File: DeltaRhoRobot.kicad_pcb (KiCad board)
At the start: 4 copper layers, 75 x 100 mm, 121 parts, among them J1 Conn_01x02_Socket, J10 Conn_01x02, J11 Conn_01x08, J12 USB_C_Receptacle_USB2.0, J13 Conn_02x09_Top_Bottom, J14 Conn_01x09, J15 Conn_02x09_Top_Bottom, J2 USB_C_Receptacle_USB2.0, J3 USB_C_Receptacle_USB2.0, J4 B4B-ZRLFSN, J5 B4B-ZRLFSN, J6 Conn_01x09, J7 Conn_02x20_Counter_Clockwise, P1 B6B-ZRLFSN, P2 B6B-ZRLFSN, P3 B6B-ZRLFSN, P4 S6B-ZRLFSN, P5 B6B-ZRLFSN, P6 B6B-ZRLFSN, Q1 MBT3904DW1, Q2 BSS138, Q3 STB55NF06T4, Q5 BSS138, SW1 CAS-120A1, SW4 SW_Push, U1 AP63205WU-7, U10 ICM-20948, U11 FT231XS, U12 ESP32-CAM, U13 MIC5365-3.3YC5, U2 AMS1117-3.3, U3 DRV8835DSSR, U4 RP2040, U5 DRV8835DSSR, U6 DRV8835DSSR, U7 W25X40CLSS, U8 ESP32-S3-WROOM-1-N8R2, Y1 ABM8G-12.000MHZ-4Y-T3

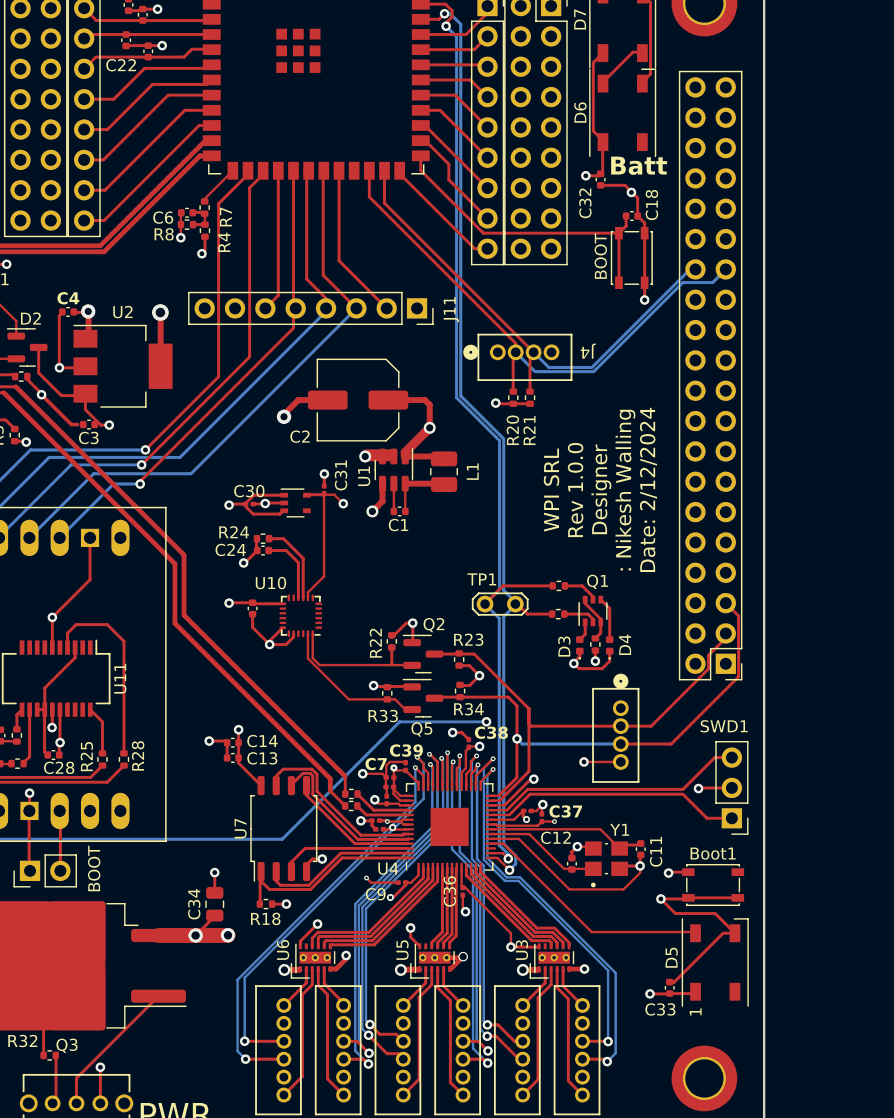
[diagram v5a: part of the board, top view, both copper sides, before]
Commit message: update to I2C
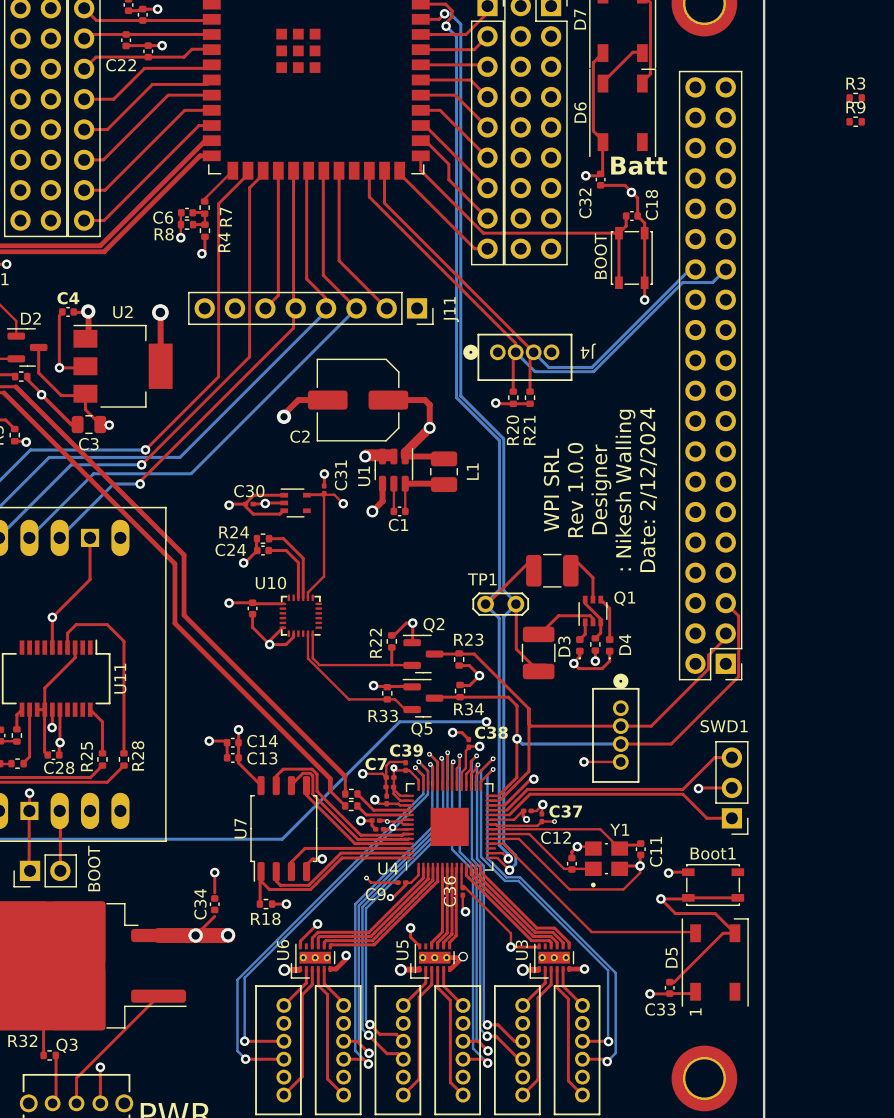
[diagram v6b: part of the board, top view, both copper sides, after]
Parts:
- added R3: 5K, Resistor_SMD:R_0402_1005Metric, F.Cu at (232.7, 62.9)
- added R9: 5K, Resistor_SMD:R_0402_1005Metric, F.Cu at (232.7, 64.9)
- C3: footprint Capacitor_SMD:C_0402_1005Metric -> Capacitor_SMD:C_0805_2012Metric
- C34: footprint Capacitor_SMD:C_0805_2012Metric -> Capacitor_SMD:C_0402_1005Metric
- R12, R13: footprint Resistor_SMD:R_0402_1005Metric -> Resistor_SMD:R_1210_3225Metric_Pad1.30x2.65mm_HandSolder
- moved R13 3.64 mm to (206.1, 109.4), turned to 90 degrees
- moved R12 1.38 mm to (207.3, 102.5)
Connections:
- R12 pad 1: ESP_TX -> Pico_SCL1
- R13 pad 1: ESP_RX -> Pico_SDA1
- R29 pad 2: Net-(U11-USBDM) -> /ESP32-S3-WROOM-1/ESP32CAM/3.3V_Out
- R30 pad 1: Net-(U11-USBDP) -> /ESP32-S3-WROOM-1/ESP32CAM/3.3V_Out
- TP1 pad 1: ESP_RX -> Pico_SDA1
- TP1 pad 2: ESP_TX -> Pico_SCL1
- U11 pad 11: Net-(U11-USBDP) -> /ESP32-S3-WROOM-1/ESP32CAM/3.3V_Out
- U11 pad 12: Net-(U11-USBDM) -> /ESP32-S3-WROOM-1/ESP32CAM/3.3V_Out
- U4 pad 15: ESP_RX -> Pico_SCL1
- U4 pad 16: ESP_TX -> Pico_SDA1
- U8 pad 36: ESP_RX -> Pico_SDA1
- U8 pad 37: ESP_TX -> Pico_SCL1
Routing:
- net Pico_SDA1: track 0.00 -> 86.7 mm, vias 0 -> 2
- net ESP_TX: track 84.7 -> 0.00 mm, vias 2 -> 0
- net Pico_SCL1: track 0.00 -> 84.3 mm, vias 0 -> 2
- net ESP_RX: track 83.2 -> 0.00 mm, vias 2 -> 0
- net /ESP32-S3-WROOM-1/ESP32CAM/3.3V_Out: track 10.8 -> 17.3 mm
- net Net-(U11-USBDM): track 4.73 -> 0.00 mm
- net Net-(Q1A-B1): track 2.85 -> 4.76 mm
- net Net-(U11-USBDP): track 1.83 -> 0.00 mm
- net Net-(Q1B-B2): track 2.97 -> 3.92 mm
- net /Pico/M6_Enc_A: track 36.2 -> 35.6 mm
- net /Pico/M6_Enc_B: track 35.9 -> 36.4 mm
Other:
- board text added: "If UART R=1k"

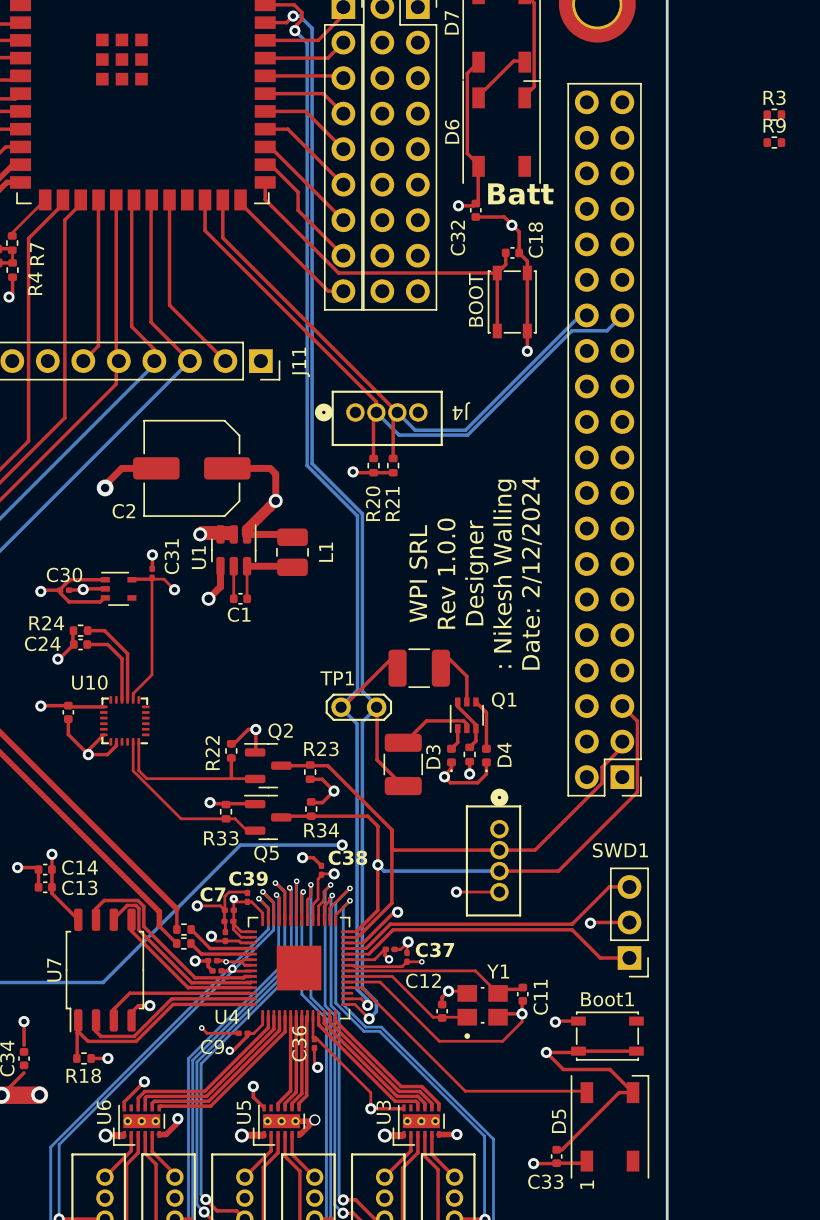
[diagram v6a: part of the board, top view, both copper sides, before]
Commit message: Fixed resistors
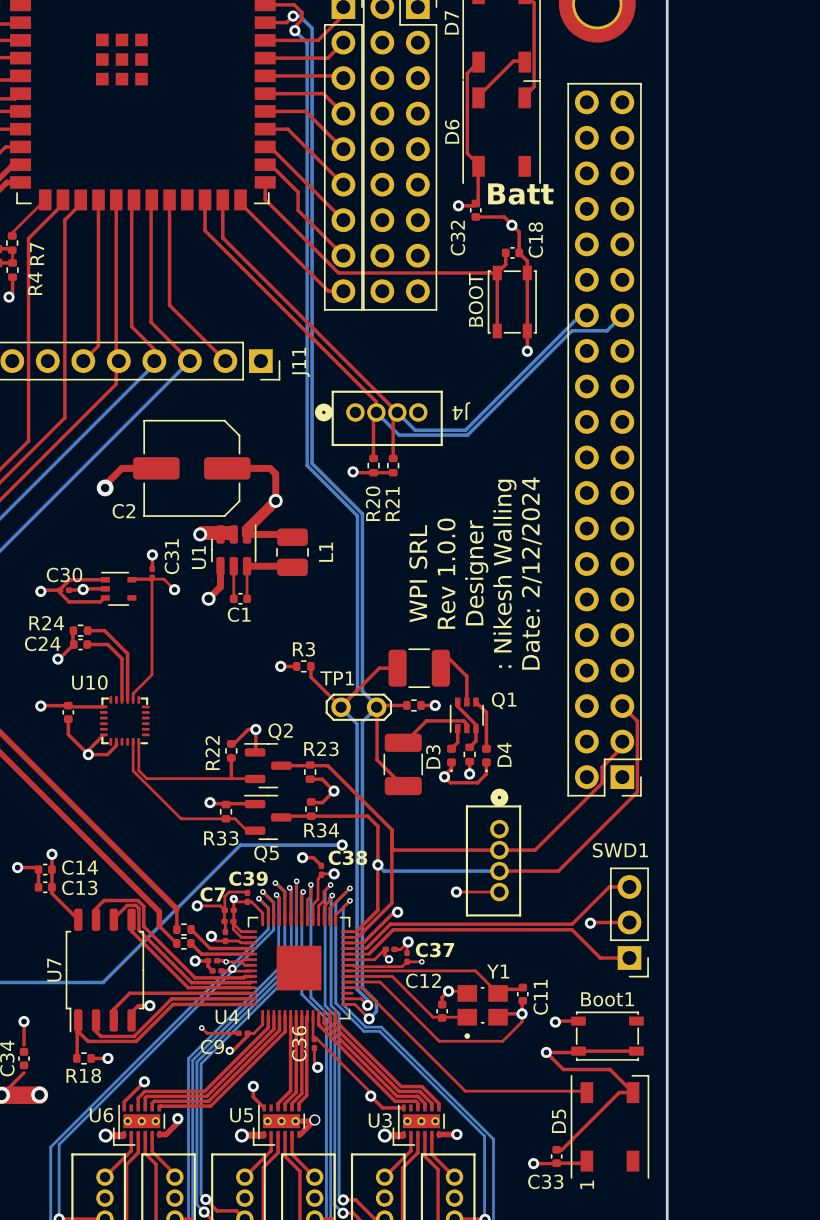
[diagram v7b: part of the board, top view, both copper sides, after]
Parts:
- moved R3 51.9 mm to (199.0, 102.4)
- moved R9 47.8 mm to (206.9, 105.2)
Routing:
- net Pico_SCL1: track 84.3 -> 87.8 mm
- net Pico_SDA1: track 86.7 -> 88.9 mm
- net +3.3V: track 85.9 -> 87.5 mm, vias 18 -> 20

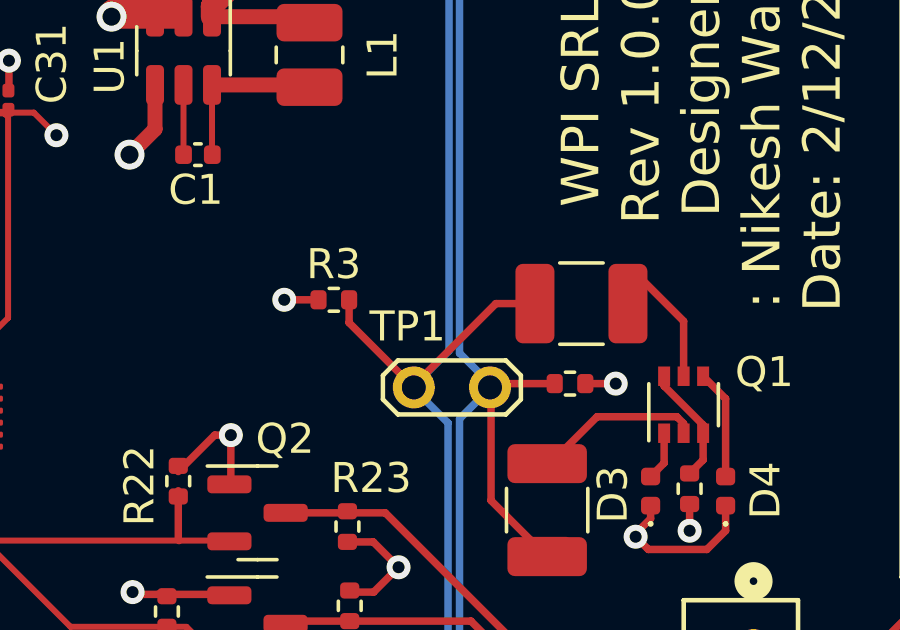
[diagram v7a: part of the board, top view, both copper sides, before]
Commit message: Fixed resistors
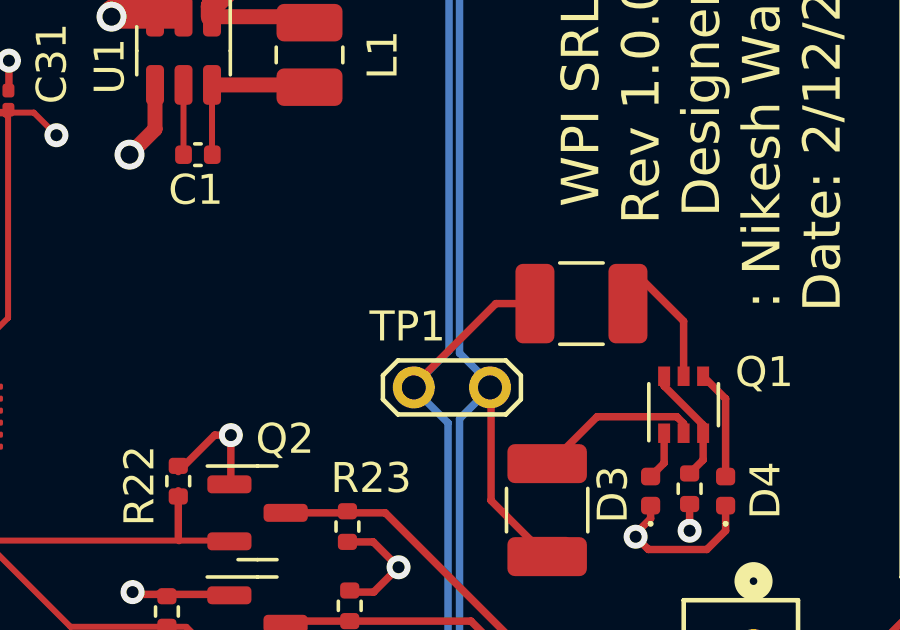
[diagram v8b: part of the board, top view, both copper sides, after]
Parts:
- removed R3, R9: 5K, Resistor_SMD:R_0402_1005Metric
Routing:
- net Pico_SCL1: track 87.8 -> 84.0 mm
- net +3.3V: track 87.5 -> 85.3 mm, vias 20 -> 18
- net Pico_SDA1: track 88.9 -> 86.9 mm
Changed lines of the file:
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@@
     )
   )
-  (footprint "Resistor_SMD:R_0402_1005Metric" (layer "F.Cu")
-    (at 206.883 105.156)
-    (descr "Resistor SMD 0402 (1005 Metric), square (rectangular) end terminal, IPC_7351 nominal, (Body size source: IPC-SM-782 page 72, https://www.pcb-3d.com/wordpress/wp-content/uploads/ipc-sm-782a_amendment_1_and_2.pdf), generated with kicad-footprint-generator")
-    (tags "resistor")
-    (property "Sheetfile" "ESP32-S3-WROOM-1.kicad_sch")
-    (property "Sheetname" "ESP32-S3-WROOM-1")
-    (property "ki_description" "Resistor, US symbol")
-    (property "ki_keywords" "R res resistor")
-    (attr smd)
-    (fp_text reference "R9" (at 0.002 -1.143) (layer "F.SilkS") hide
-        (effects (font (size 1 1) (thickness 0.15)))
-    )
-    (fp_text value "5K" (at 0 1.17) (layer "F.Fab")
-        (effects (font (size 1 1) (thickness 0.15)))
-    )
-    (fp_text user "${REFERENCE}" (at 0 0) (layer "F.Fab")
-        (effects (font (size 0.26 0.26) (thickness 0.04)))
-    )
-    (fp_line (start -0.153641 -0.38) (end 0.153641 -0.38)
-      (stroke (width 0.12) (type solid)) (layer "F.SilkS"))
-    (fp_line (start -0.153641 0.38) (end 0.153641 0.38)
-      (stroke (width 0.12) (type solid)) (layer "F.SilkS"))
-    (fp_line (start -0.93 -0.47) (end 0.93 -0.47)
-      (stroke (width 0.05) (type solid)) (layer "F.CrtYd"))
-    (fp_line (start -0.93 0.47) (end -0.93 -0.47)
-      (stroke (width 0.05) (type solid)) (layer "F.CrtYd"))
-    (fp_line (start 0.93 -0.47) (end 0.93 0.47)
-      (stroke (width 0.05) (type solid)) (layer "F.CrtYd"))
-    (fp_line (start 0.93 0.47) (end -0.93 0.47)
-      (stroke (width 0.05) (type solid)) (layer "F.CrtYd"))
-    (fp_line (start -0.525 -0.27) (end 0.525 -0.27)
-      (stroke (width 0.1) (type solid)) (layer "F.Fab"))
-    (fp_line (start -0.525 0.27) (end -0.525 -0.27)
-      (stroke (width 0.1) (type solid)) (layer "F.Fab"))
-    (fp_line (start 0.525 -0.27) (end 0.525 0.27)
-      (stroke (width 0.1) (type solid)) (layer "F.Fab"))
-    (fp_line (start 0.525 0.27) (end -0.525 0.27)
-      (stroke (width 0.1) (type solid)) (layer "F.Fab"))
-    (pad "1" smd roundrect (at -0.51 0) (size 0.54 0.64) (layers "F.Cu" "F.Paste" "F.Mask") (roundrect_rratio 0.25)
-      (net 200 "Pico_SDA1") (pintype "passive"))
-    (pad "2" smd roundrect (at 0.51 0) (size 0.54 0.64) (layers "F.Cu" "F.Paste" "F.Mask") (roundrect_rratio 0.25)
-      (net 146 "+3.3V") (pintype "passive"))
-    (model "${KICAD6_3DMODEL_DIR}/Resistor_SMD.3dshapes/R_0402_1005Metric.wrl"
-      (offset (xyz 0 0 0))
-      (scale (xyz 1 1 1))
-      (rotate (xyz 0 0 0))
-    )
-  )
   (footprint "Capacitor_SMD:C_0402_1005Metric" (layer "F.Cu")
     (at 214.6702 125.8047 -90)
@@
   )
   (footprint "Resistor_SMD:R_0402_1005Metric" (layer "F.Cu")
-    (at 199.009 102.362)
-    (descr "Resistor SMD 0402 (1005 Metric), square (rectangular) end terminal, IPC_7351 nominal, (Body size source: IPC-SM-782 page 72, https://www.pcb-3d.com/wordpress/wp-content/uploads/ipc-sm-782a_amendment_1_and_2.pdf), generated with kicad-footprint-generator")
-    (tags "resistor")
-    (property "Sheetfile" "ESP32-S3-WROOM-1.kicad_sch")
-    (property "Sheetname" "ESP32-S3-WROOM-1")
-    (property "ki_description" "Resistor, US symbol")
-    (property "ki_keywords" "R res resistor")
-    (attr smd)
-    (fp_text reference "R3" (at -0.002 -1.185) (layer "F.SilkS")
-        (effects (font (size 1 1) (thickness 0.15)))
-    )
-    (fp_text value "5K" (at 0 1.17) (layer "F.Fab")
-        (effects (font (size 1 1) (thickness 0.15)))
-    )
-    (fp_text user "${REFERENCE}" (at 0 0) (layer "F.Fab")
-        (effects (font (size 0.26 0.26) (thickness 0.04)))
-    )
-    (fp_line (start -0.153641 -0.38) (end 0.153641 -0.38)
-      (stroke (width 0.12) (type solid)) (layer "F.SilkS"))
-    (fp_line (start -0.153641 0.38) (end 0.153641 0.38)
-      (stroke (width 0.12) (type solid)) (layer "F.SilkS"))
-    (fp_line (start -0.93 -0.47) (end 0.93 -0.47)
-      (stroke (width 0.05) (type solid)) (layer "F.CrtYd"))
-    (fp_line (start -0.93 0.47) (end -0.93 -0.47)
-      (stroke (width 0.05) (type solid)) (layer "F.CrtYd"))
-    (fp_line (start 0.93 -0.47) (end 0.93 0.47)
-      (stroke (width 0.05) (type solid)) (layer "F.CrtYd"))
-    (fp_line (start 0.93 0.47) (end -0.93 0.47)
-      (stroke (width 0.05) (type solid)) (layer "F.CrtYd"))
-    (fp_line (start -0.525 -0.27) (end 0.525 -0.27)
-      (stroke (width 0.1) (type solid)) (layer "F.Fab"))
-    (fp_line (start -0.525 0.27) (end -0.525 -0.27)
-      (stroke (width 0.1) (type solid)) (layer "F.Fab"))
-    (fp_line (start 0.525 -0.27) (end 0.525 0.27)
-      (stroke (width 0.1) (type solid)) (layer "F.Fab"))
-    (fp_line (start 0.525 0.27) (end -0.525 0.27)
-      (stroke (width 0.1) (type solid)) (layer "F.Fab"))
-    (pad "1" smd roundrect (at -0.51 0) (size 0.54 0.64) (layers "F.Cu" "F.Paste" "F.Mask") (roundrect_rratio 0.25)
-      (net 146 "+3.3V") (pintype "passive"))
-    (pad "2" smd roundrect (at 0.51 0) (size 0.54 0.64) (layers "F.Cu" "F.Paste" "F.Mask") (roundrect_rratio 0.25)
-      (net 196 "Pico_SCL1") (pintype "passive"))
-    (model "${KICAD6_3DMODEL_DIR}/Resistor_SMD.3dshapes/R_0402_1005Metric.wrl"
-      (offset (xyz 0 0 0))
-      (scale (xyz 1 1 1))
-      (rotate (xyz 0 0 0))
-    )
-  )
-  (footprint "Resistor_SMD:R_0402_1005Metric" (layer "F.Cu")
     (at 190.44 121.18 180)
     (descr "Resistor SMD 0402 (1005 Metric), square (rectangular) end terminal, IPC_7351 nominal, (Body size source: IPC-SM-782 page 72, https://www.pcb-3d.com/wordpress/wp-content/uploads/ipc-sm-782a_amendment_1_and_2.pdf), generated with kicad-footprint-generator")
@@
   (segment (start 184.706 105.2576) (end 182.1478 105.2576) (width 0.25) (layer "F.Cu") (net 146))
   (segment (start 180.2 105.2) (end 180.232 105.168) (width 0.25) (layer "F.Cu") (net 146))
-  (segment (start 208.407 105.156) (end 207.393 105.156) (width 0.25) (layer "F.Cu") (net 146))
   (segment (start 165.989 85.489) (end 165.989 81.151) (width 0.25) (layer "F.Cu") (net 146))
   (segment (start 192.805 123.41) (end 193.37 123.41) (width 0.25) (layer "F.Cu") (net 146))
   (segment (start 187.61 132.07) (end 186.1688 133.5112) (width 0.25) (layer "F.Cu") (net 146))
   (segment (start 194.7938 123.7372) (end 195.2313 123.7372) (width 0.2) (layer "F.Cu") (net 146))
-  (segment (start 197.358 102.362) (end 198.499 102.362) (width 0.25) (layer "F.Cu") (net 146))
   (segment (start 199.6688 128.9188) (end 199.6688 127.3747) (width 0.2) (layer "F.Cu") (net 146))
   (segment (start 180.9978 118.1608) (end 180.9978 116.8934) (width 0.25) (layer "F.Cu") (net 146))
@@
   (via (at 166 85.5) (size 0.8) (drill 0.4) (layers "F.Cu" "B.Cu") (free) (net 146))
   (via (at 174.45 80.87) (size 1.4) (drill 0.8) (layers "F.Cu" "B.Cu") (free) (net 146))
-  (via (at 197.358 102.362) (size 0.8) (drill 0.4) (layers "F.Cu" "B.Cu") (free) (net 146))
   (via (at 201.18 117.2) (size 0.8) (drill 0.4) (layers "F.Cu" "B.Cu") (free) (net 146))
   (via (at 180.2 97) (size 0.8) (drill 0.4) (layers "F.Cu" "B.Cu") (net 146))
@@
   (via (at 203.8 133.096) (size 0.8) (drill 0.4) (layers "F.Cu" "B.Cu") (free) (net 146))
   (via (at 175.5608 52.158987) (size 0.8) (drill 0.4) (layers "F.Cu" "B.Cu") (free) (net 146))
-  (via (at 208.407 105.156) (size 0.8) (drill 0.4) (layers "F.Cu" "B.Cu") (free) (net 146))
   (via (at 180.2 105.2) (size 0.8) (drill 0.4) (layers "F.Cu" "B.Cu") (remove_unused_layers) (free) (zone_layer_connections "In2.Cu") (net 146))
   (via (at 207.45 123.49) (size 0.4) (drill 0.2) (layers "F.Cu" "B.Cu") (free) (net 146))
@@
   (segment (start 198.872 55.595716) (end 198.326284 55.05) (width 0.25) (layer "F.Cu") (net 196))
   (segment (start 203.57735 126.60502) (end 203.10953 126.1372) (width 0.2) (layer "F.Cu") (net 196))
-  (segment (start 201.676 105.283) (end 199.519 103.126) (width 0.25) (layer "F.Cu") (net 196))
   (segment (start 198.505884 56.764116) (end 198.505884 56.4796) (width 0.25) (layer "F.Cu") (net 196))
   (segment (start 198.374 56.896) (end 198.505884 56.764116) (width 0.25) (layer "F.Cu") (net 196))
@@
   (segment (start 201.71 105.19) (end 204.411 102.489) (width 0.25) (layer "F.Cu") (net 196))
   (segment (start 203.10953 126.1372) (end 202.1063 126.1372) (width 0.2) (layer "F.Cu") (net 196))
-  (segment (start 199.519 103.126) (end 199.519 102.362) (width 0.25) (layer "F.Cu") (net 196))
   (via (at 203.57735 126.60502) (size 0.8) (drill 0.4) (layers "F.Cu" "B.Cu") (free) (net 196))
   (via (at 198.374 56.896) (size 0.8) (drill 0.4) (layers "F.Cu" "B.Cu") (free) (net 196))
@@
   (segment (start 205.587 110.389) (end 204.25 109.052) (width 0.25) (layer "F.Cu") (net 200))
   (segment (start 204.343 105.156) (end 204.216 105.283) (width 0.25) (layer "F.Cu") (net 200))
-  (segment (start 206.373 105.156) (end 204.343 105.156) (width 0.25) (layer "F.Cu") (net 200))
   (segment (start 202.661 126.5372) (end 203.6826 127.5588) (width 0.2) (layer "F.Cu") (net 200))
   (segment (start 204.25 109.052) (end 204.25 105.19) (width 0.25) (layer "F.Cu") (net 200))
